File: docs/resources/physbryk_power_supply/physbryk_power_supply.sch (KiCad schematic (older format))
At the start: 7 parts, among them U1 LM317_TO-220

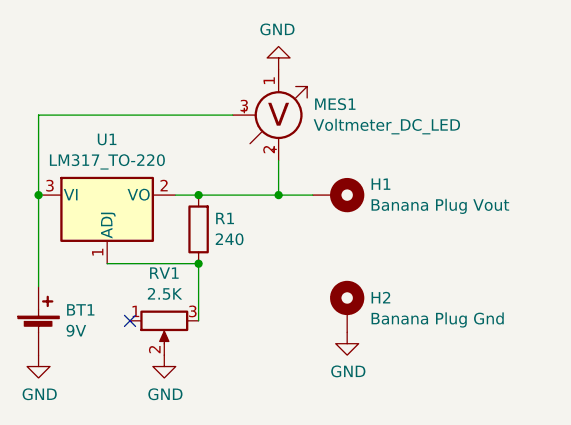
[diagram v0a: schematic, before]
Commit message: added kicad files for the power supply
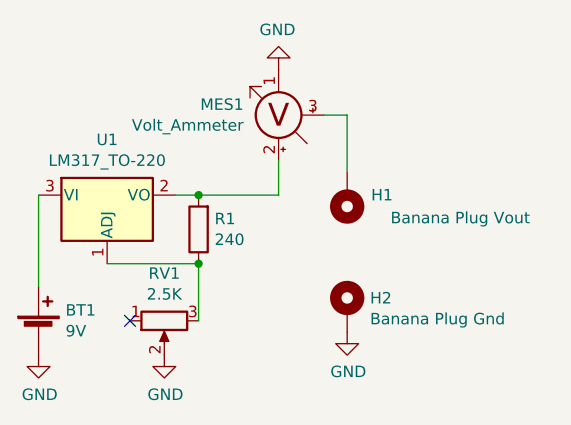
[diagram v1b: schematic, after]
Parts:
- MES1: value Voltmeter_DC_LED -> Volt_Ammeter
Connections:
- net at MES1.2 (Vtarget), R1.2, U1.2 (VO): no longer H1.1
- net at BT1.1 (+), U1.3 (VI): no longer MES1.3 (Vin)
- new net: H1.1, MES1.3 (Vin)
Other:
- moved on the sheet: H1, MES1
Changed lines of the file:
@@
-$EndComp
-$Comp
-L physbryk_symbol:MountingHole_Pad H1
-U 1 1 5F9025E3
-P 7450 2600
-F 0 "H1" V 7404 2750 50  0000 L CNN
-F 1 "Banana Plug Vout" V 7495 2750 50  0000 L CNN
-F 2 "Connector:Banana_Jack_1Pin" H 7450 2600 50  0001 C CNN
-F 3 "~" H 7450 2600 50  0001 C CNN
-	1    7450 2600
-	0    1    1    0
 $EndComp
 $Comp
@@
 	0    -1   1    0
 $EndComp
-Connection ~ 6850 2600
 Wire Wire Line
 	6850 2900 6850 3150
@@
 $EndComp
 Wire Wire Line
+	7200 2450 7200 2600
+Connection ~ 6850 2600
+Wire Wire Line
 	6850 2600 7200 2600
-Wire Wire Line
-	7200 2450 7200 2600
-Connection ~ 7200 2600
-Wire Wire Line
-	7200 2600 7350 2600
-Wire Wire Line
-	7000 2250 6150 2250
-Wire Wire Line
-	6150 2250 6150 2600
-Connection ~ 6150 2600
 $Comp
 L physbryk_power_supply-rescue:Voltmeter_DC_LED-physbryk_symbol MES1
@@
 P 7200 2250
 F 0 "MES1" H 7353 2296 50  0000 L CNN
-F 1 "Voltmeter_DC_LED" H 7353 2205 50  0000 L CNN
+F 1 "Volt_Ammeter" H 7353 2205 50  0000 L CNN
 F 2 "Connector_Wire:SolderWire-0.5sqmm_1x03_P4.8mm_D0.9mm_OD2.3mm" V 7200 2350 50  0001 C CNN
 F 3 "~" V 7200 2350 50  0001 C CNN
 	1    7200 2250
-	1    0    0    -1
+	-1   0    0    -1
 $EndComp
+$Comp
+L physbryk_symbol:MountingHole_Pad H1
+U 1 1 5F9025E3
+P 7500 2600
+F 0 "H1" H 7300 2600 50  0000 L CNN
+F 1 "Banana Plug Vout" H 6700 2700 50  0000 L CNN
+F 2 "Connector:Banana_Jack_1Pin" H 7500 2600 50  0001 C CNN
+F 3 "~" H 7500 2600 50  0001 C CNN
+	1    7500 2600
+	-1   0    0    1
+$EndComp
+Wire Wire Line
+	7500 2500 7500 2250
+Wire Wire Line
+	7500 2250 7400 2250
 $EndSCHEMATC
